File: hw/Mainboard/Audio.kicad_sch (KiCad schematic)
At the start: 12 parts, among them J1 SJ-43504-SMT-TR, J8 SPEAKER, Q2 MMBT3904

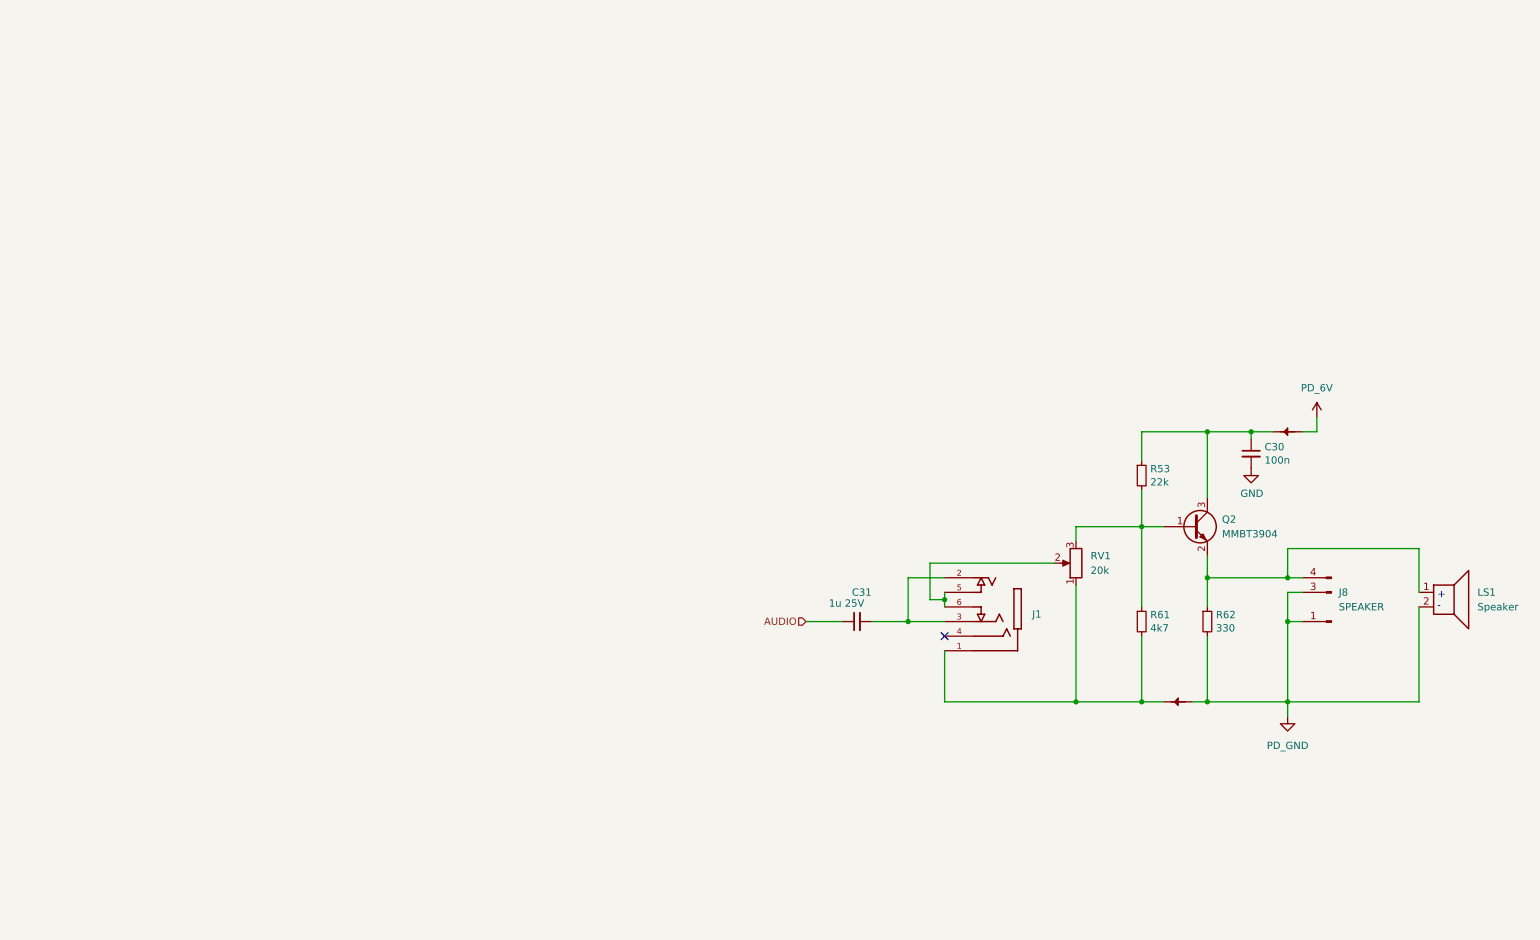
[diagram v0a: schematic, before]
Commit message: hw: tidy power and resize pages
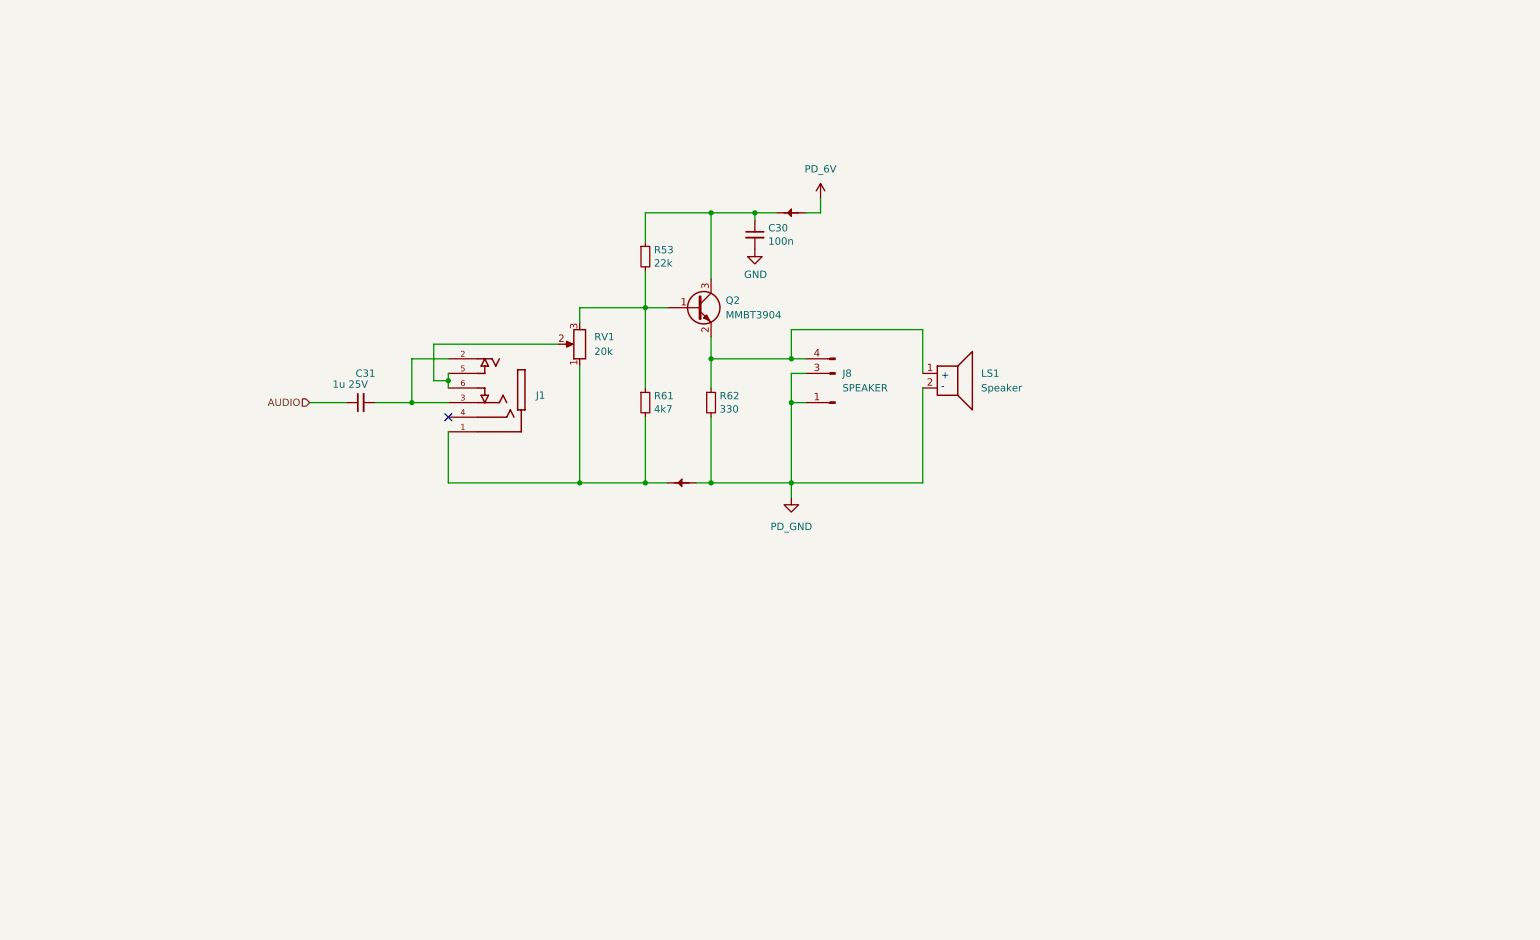
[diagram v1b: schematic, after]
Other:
- title: Audio -> CBM PET Mainboard Replacement
- moved on the sheet: C30, C31, J1, J8, LS1, Q2, R53, R61, R62, RV1

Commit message: hw: tidy audio, cass, IEEE, keyboard, magic, user
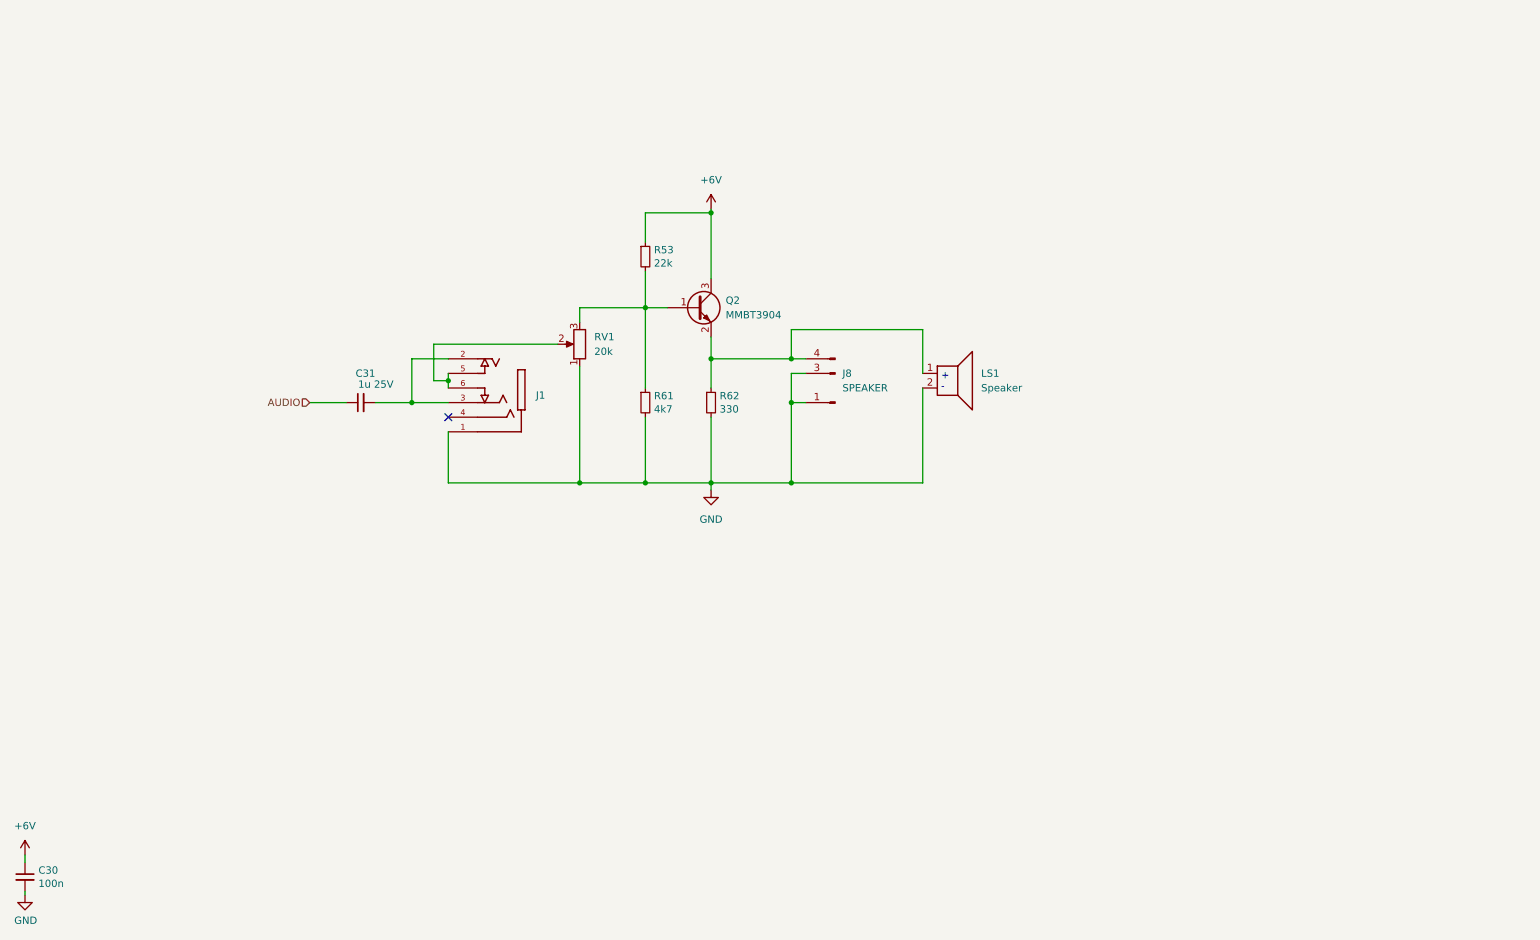
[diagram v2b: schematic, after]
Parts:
- removed NT24: GND, PET:NetTie-2_SMD_Pad_1.6_to_0.4mm, symbol PET:PowerTie_2
- removed NT9: +6V, PET:NetTie-2_SMD_Pad_1.6_to_0.4mm, symbol PET:PowerTie_2
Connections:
- net PD_GND is gone; now on net GND: J8.1 (Pin_1), J8.3 (Pin_3), LS1.2, R62.2
- net GND: now also J1.1, R61.2, RV1.1
- net +6V: now reaches C30.1, Q2.3 (C), R53.1
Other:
- moved on the sheet: C30
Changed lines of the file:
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@@
   (junction (at 104.14 99.06) (diameter 0) (color 0 0 0 0)
   )
+  (junction (at 149.86 69.85) (diameter 0) (color 0 0 0 0)
+  )
   (junction (at 127 116.84) (diameter 0) (color 0 0 0 0)
   )
   (junction (at 138.43 116.84) (diameter 0) (color 0 0 0 0)
   )
-  (junction (at 149.86 69.85) (diameter 0) (color 0 0 0 0)
-  )
   (junction (at 149.86 116.84) (diameter 0) (color 0 0 0 0)
-  )
-  (junction (at 157.48 69.85) (diameter 0) (color 0 0 0 0)
   )
   (junction (at 163.83 102.87) (diameter 0) (color 0 0 0 0)
@@
     (stroke (width 0) (type default) (color 0 0 0 0))
   )
+  (wire (pts (xy 149.86 69.215) (xy 149.86 69.85))
+    (stroke (width 0) (type default) (color 0 0 0 0))
+  )
   (wire (pts (xy 138.43 80.01) (xy 138.43 86.36))
     (stroke (width 0) (type default) (color 0 0 0 0))
@@
     (stroke (width 0) (type default) (color 0 0 0 0))
   )
-  (wire (pts (xy 157.48 69.85) (xy 157.48 71.12))
+  (wire (pts (xy 30.48 181.61) (xy 30.48 182.88))
     (stroke (width 0) (type default) (color 0 0 0 0))
   )
@@
     (stroke (width 0) (type default) (color 0 0 0 0))
   )
-  (wire (pts (xy 138.43 116.84) (xy 142.24 116.84))
+  (wire (pts (xy 138.43 116.84) (xy 149.86 116.84))
     (stroke (width 0) (type default) (color 0 0 0 0))
   )
@@
     (stroke (width 0) (type default) (color 0 0 0 0))
   )
-  (wire (pts (xy 168.91 69.85) (xy 166.37 69.85))
-    (stroke (width 0) (type default) (color 0 0 0 0))
-  )
-  (wire (pts (xy 161.29 69.85) (xy 157.48 69.85))
-    (stroke (width 0) (type default) (color 0 0 0 0))
-  )
   (wire (pts (xy 97.79 102.87) (xy 104.14 102.87))
     (stroke (width 0) (type default) (color 0 0 0 0))
@@
     (stroke (width 0) (type default) (color 0 0 0 0))
   )
-  (wire (pts (xy 157.48 69.85) (xy 149.86 69.85))
-    (stroke (width 0) (type default) (color 0 0 0 0))
-  )
-  (wire (pts (xy 163.83 116.84) (xy 163.83 119.38))
-    (stroke (width 0) (type default) (color 0 0 0 0))
-  )
-  (wire (pts (xy 168.91 67.31) (xy 168.91 69.85))
-    (stroke (width 0) (type default) (color 0 0 0 0))
-  )
   (wire (pts (xy 127 116.84) (xy 138.43 116.84))
     (stroke (width 0) (type default) (color 0 0 0 0))
@@
     (stroke (width 0) (type default) (color 0 0 0 0))
   )
-  (wire (pts (xy 147.32 116.84) (xy 149.86 116.84))
-    (stroke (width 0) (type default) (color 0 0 0 0))
-  )
   (wire (pts (xy 186.69 100.33) (xy 186.69 116.84))
     (stroke (width 0) (type default) (color 0 0 0 0))
   )
+  (wire (pts (xy 149.86 118.11) (xy 149.86 116.84))
+    (stroke (width 0) (type default) (color 0 0 0 0))
+  )
   (wire (pts (xy 104.14 99.06) (xy 104.14 100.33))
     (stroke (width 0) (type default) (color 0 0 0 0))
@@
   )
   (wire (pts (xy 138.43 86.36) (xy 142.24 86.36))
+    (stroke (width 0) (type default) (color 0 0 0 0))
+  )
+  (wire (pts (xy 30.48 188.595) (xy 30.48 187.96))
     (stroke (width 0) (type default) (color 0 0 0 0))
   )
@@
     (effects (font (size 1.27 1.27)) (justify right))
   )
-  (symbol (lib_id "Device:C_Small") (at 157.48 73.66 0) (unit 1)
-    (in_bom yes) (on_board yes)
-    (property "Reference" "C30" (id 0) (at 159.8168 72.4916 0)
-      (effects (font (size 1.27 1.27)) (justify left))
-    )
-    (property "Value" "100n" (id 1) (at 159.8168 74.803 0)
-      (effects (font (size 1.27 1.27)) (justify left))
-    )
-    (property "Footprint" "Capacitor_SMD:C_0402_1005Metric" (id 2) (at 157.48 73.66 0)
-      (effects (font (size 1.27 1.27)) hide)
-    )
-    (property "Datasheet" "https://datasheet.lcsc.com/lcsc/1810191219_Samsung-Electro-Mechanics-CL05B104KO5NNNC_C1525.pdf" (id 3) (at 157.48 73.66 0)
-      (effects (font (size 1.27 1.27)) hide)
-    )
-    (property "LCSC" "C1525" (id 4) (at 157.48 73.66 0)
-      (effects (font (size 1.27 1.27)) hide)
-    )
-    (pin "1")
-    (pin "2")
-  )
-  (symbol (lib_id "PET:PowerTie_2") (at 144.78 116.84 0) (mirror y) (unit 1)
-    (in_bom yes) (on_board yes)
-    (property "Reference" "NT24" (id 0) (at 144.78 114.3 0)
-      (effects (font (size 1.27 1.27)) hide)
-    )
-    (property "Value" "GND" (id 1) (at 144.78 114.3 0)
-      (effects (font (size 1.27 1.27)) hide)
-    )
-    (property "Footprint" "PET:NetTie-2_SMD_Pad_1.6_to_0.4mm" (id 2) (at 144.78 116.84 0)
-      (effects (font (size 1.27 1.27)) hide)
-    )
-    (property "Datasheet" "~" (id 3) (at 144.78 116.84 0)
+  (symbol (lib_id "Device:C_Small") (at 30.48 185.42 0) (unit 1)
+    (in_bom yes) (on_board yes)
+    (property "Reference" "C30" (id 0) (at 32.8168 184.2516 0)
+      (effects (font (size 1.27 1.27)) (justify left))
+    )
+    (property "Value" "100n" (id 1) (at 32.8168 186.563 0)
+      (effects (font (size 1.27 1.27)) (justify left))
+    )
+    (property "Footprint" "Capacitor_SMD:C_0402_1005Metric" (id 2) (at 30.48 185.42 0)
+      (effects (font (size 1.27 1.27)) hide)
+    )
+    (property "Datasheet" "https://datasheet.lcsc.com/lcsc/1810191219_Samsung-Electro-Mechanics-CL05B104KO5NNNC_C1525.pdf" (id 3) (at 30.48 185.42 0)
+      (effects (font (size 1.27 1.27)) hide)
+    )
+    (property "LCSC" "C1525" (id 4) (at 30.48 185.42 0)
       (effects (font (size 1.27 1.27)) hide)
     )
@@
     (pin "1")
     (pin "2")
-  )
-  (symbol (lib_id "PET:PD_GND") (at 163.83 119.38 0) (unit 1)
-    (in_bom yes) (on_board yes) (fields_autoplaced)
-    (property "Reference" "#PWR0220" (id 0) (at 163.83 125.73 0)
-      (effects (font (size 1.27 1.27)) hide)
-    )
-    (property "Value" "PD_GND" (id 1) (at 163.83 124.46 0))
-    (property "Footprint" "" (id 2) (at 163.83 119.38 0)
-      (effects (font (size 1.27 1.27)) hide)
-    )
-    (property "Datasheet" "" (id 3) (at 163.83 119.38 0)
-      (effects (font (size 1.27 1.27)) hide)
-    )
-    (pin "1")
   )
   (symbol (lib_id "Transistor_BJT:MMBT3904") (at 147.32 86.36 0) (unit 1)
@@
     (pin "6")
   )
-  (symbol (lib_id "power:GND") (at 157.48 76.2 0) (unit 1)
-    (in_bom yes) (on_board yes)
-    (property "Reference" "#PWR0126" (id 0) (at 157.48 82.55 0)
-      (effects (font (size 1.27 1.27)) hide)
-    )
-    (property "Value" "GND" (id 1) (at 157.607 80.5942 0))
-    (property "Footprint" "" (id 2) (at 157.48 76.2 0)
-      (effects (font (size 1.27 1.27)) hide)
-    )
-    (property "Datasheet" "" (id 3) (at 157.48 76.2 0)
-      (effects (font (size 1.27 1.27)) hide)
-    )
-    (pin "1")
-  )
-  (symbol (lib_id "PET:PowerTie_2") (at 163.83 69.85 0) (mirror y) (unit 1)
-    (in_bom yes) (on_board yes)
-    (property "Reference" "NT9" (id 0) (at 163.83 67.31 0)
-      (effects (font (size 1.27 1.27)) hide)
-    )
-    (property "Value" "+6V" (id 1) (at 163.83 67.31 0)
-      (effects (font (size 1.27 1.27)) hide)
-    )
-    (property "Footprint" "PET:NetTie-2_SMD_Pad_1.6_to_0.4mm" (id 2) (at 163.83 69.85 0)
-      (effects (font (size 1.27 1.27)) hide)
-    )
-    (property "Datasheet" "~" (id 3) (at 163.83 69.85 0)
-      (effects (font (size 1.27 1.27)) hide)
-    )
-    (pin "1")
-    (pin "2")
+  (symbol (lib_id "power:GND") (at 30.48 188.595 0) (unit 1)
+    (in_bom yes) (on_board yes)
+    (property "Reference" "#PWR0126" (id 0) (at 30.48 194.945 0)
+      (effects (font (size 1.27 1.27)) hide)
+    )
+    (property "Value" "GND" (id 1) (at 30.607 192.9892 0))
+    (property "Footprint" "" (id 2) (at 30.48 188.595 0)
+      (effects (font (size 1.27 1.27)) hide)
+    )
+    (property "Datasheet" "" (id 3) (at 30.48 188.595 0)
+      (effects (font (size 1.27 1.27)) hide)
+    )
+    (pin "1")
+  )
+  (symbol (lib_id "power:GND") (at 149.86 118.11 0) (unit 1)
+    (in_bom yes) (on_board yes) (fields_autoplaced)
+    (property "Reference" "#PWR?" (id 0) (at 149.86 124.46 0)
+      (effects (font (size 1.27 1.27)) hide)
+    )
+    (property "Value" "GND" (id 1) (at 149.86 123.19 0))
+    (property "Footprint" "" (id 2) (at 149.86 118.11 0)
+      (effects (font (size 1.27 1.27)) hide)
+    )
+    (property "Datasheet" "" (id 3) (at 149.86 118.11 0)
+      (effects (font (size 1.27 1.27)) hide)
+    )
+    (pin "1")
+  )
+  (symbol (lib_id "power:+6V") (at 30.48 181.61 0) (unit 1)
+    (in_bom yes) (on_board yes) (fields_autoplaced)
+    (property "Reference" "#PWR?" (id 0) (at 30.48 185.42 0)
+      (effects (font (size 1.27 1.27)) hide)
+    )
+    (property "Value" "+6V" (id 1) (at 30.48 176.53 0))
+    (property "Footprint" "" (id 2) (at 30.48 181.61 0)
+      (effects (font (size 1.27 1.27)) hide)
+    )
+    (property "Datasheet" "" (id 3) (at 30.48 181.61 0)
+      (effects (font (size 1.27 1.27)) hide)
+    )
+    (pin "1")
   )
   (symbol (lib_id "Device:R_Small") (at 138.43 102.87 0) (unit 1)
@@
       (effects (font (size 1.27 1.27)) (justify left))
     )
-    (property "Value" "1u 25V" (id 1) (at 90.17 99.695 90)
+    (property "Value" "1u 25V" (id 1) (at 94.615 99.695 90)
       (effects (font (size 1.27 1.27)) (justify left))
     )
@@
     (pin "2")
   )
-  (symbol (lib_id "PET:PD_6V") (at 168.91 67.31 0) (unit 1)
-    (in_bom yes) (on_board yes)
-    (property "Reference" "#PWR0197" (id 0) (at 168.91 71.12 0)
-      (effects (font (size 1.27 1.27)) hide)
-    )
-    (property "Value" "PD_6V" (id 1) (at 168.91 62.23 0))
-    (property "Footprint" "" (id 2) (at 168.91 67.31 0)
-      (effects (font (size 1.27 1.27)) hide)
-    )
-    (property "Datasheet" "" (id 3) (at 168.91 67.31 0)
-      (effects (font (size 1.27 1.27)) hide)
-    )
+  (symbol (lib_id "power:+6V") (at 149.86 69.215 0) (unit 1)
+    (in_bom yes) (on_board yes) (fields_autoplaced)
+    (property "Reference" "#PWR?" (id 0) (at 149.86 73.025 0)
+      (effects (font (size 1.27 1.27)) hide)
+    )
+    (property "Value" "+6V" (id 1) (at 149.86 64.135 0))
+    (property "Footprint" "" (id 2) (at 149.86 69.215 0)
+      (effects (font (size 1.27 1.27)) hide)
+    )
+    (property "Datasheet" "" (id 3) (at 149.86 69.215 0)
+      (effects (font (size 1.27 1.27)) hide)
+    )

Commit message: hw: wip
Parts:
- added PT26: PowerTie_2, PET:NetTie-2_SMD_Pad_1.6_to_0.4mm, symbol PET:PowerTie_2
- C31: value 1u 25V -> 1u
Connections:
- net +6V: now also PT26.1; no longer C30.1, Q2.3 (C), R53.1
- new net: C30.1, PT26.2, Q2.3 (C), R53.1
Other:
- note added: "Note: The AUDIO signal is a 3V3 square wave rather than 5V as on original models. This is because the CB2 output of the VIA is routed through spare pins on the FPGA to implement the NAND with DIAG."
- moved on the sheet: C30, C31, J1, J8, LS1, Q2, R53, R61, R62, RV1

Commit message: wip: keyboard ex header
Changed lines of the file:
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@@
-    (stroke (width 0) (type default) (color 0 0 0 0))
-  )
-  (wire (pts (xy 30.48 181.61) (xy 30.48 182.88))
     (stroke (width 0) (type default) (color 0 0 0 0))
   )
@@
     (pin "2")
   )
-  (symbol (lib_id "power:+6V") (at 30.48 181.61 0) (unit 1)
-    (in_bom yes) (on_board yes) (fields_autoplaced)
-    (property "Reference" "#PWR0138" (id 0) (at 30.48 185.42 0)
-      (effects (font (size 1.27 1.27)) hide)
-    )
-    (property "Value" "+6V" (id 1) (at 30.48 176.53 0))
-    (property "Footprint" "" (id 2) (at 30.48 181.61 0)
-      (effects (font (size 1.27 1.27)) hide)
-    )
-    (property "Datasheet" "" (id 3) (at 30.48 181.61 0)
-      (effects (font (size 1.27 1.27)) hide)
-    )
-    (pin "1")
-  )
   (symbol (lib_id "Device:R_Small") (at 147.32 101.6 0) (unit 1)
